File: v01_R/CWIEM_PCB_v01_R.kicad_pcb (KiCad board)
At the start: 2 copper layers, 50.8 x 50.8 mm, 46 parts, among them J1 USB, P1 CONN_1, P10 CONN_1, P11 CONN_1, P12 CONN_1, P2 CONN_1, P7 CONN_1, P8 CONN_1, P9 CONN_1, Q3 PNP, SW1 SW_PUSH_SMALL, U1 BC127, U2 TI_TPA6138A2, U4 MIC5219

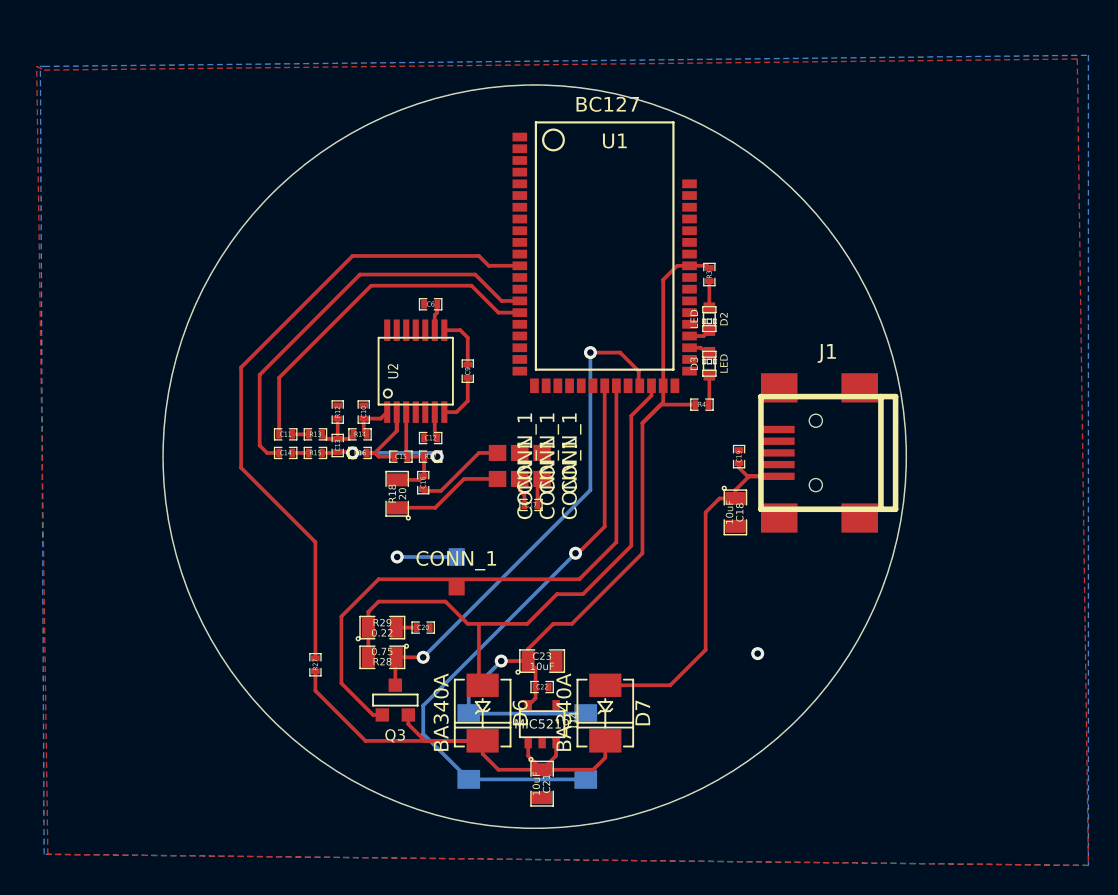
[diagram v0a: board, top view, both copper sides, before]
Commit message: Update with 2.00" diameter version of the CWIEM R v01 PCB. The only change remaining was to finalize sound driver pad placement and sizing. After that, production files could be generated for board manufacturing.
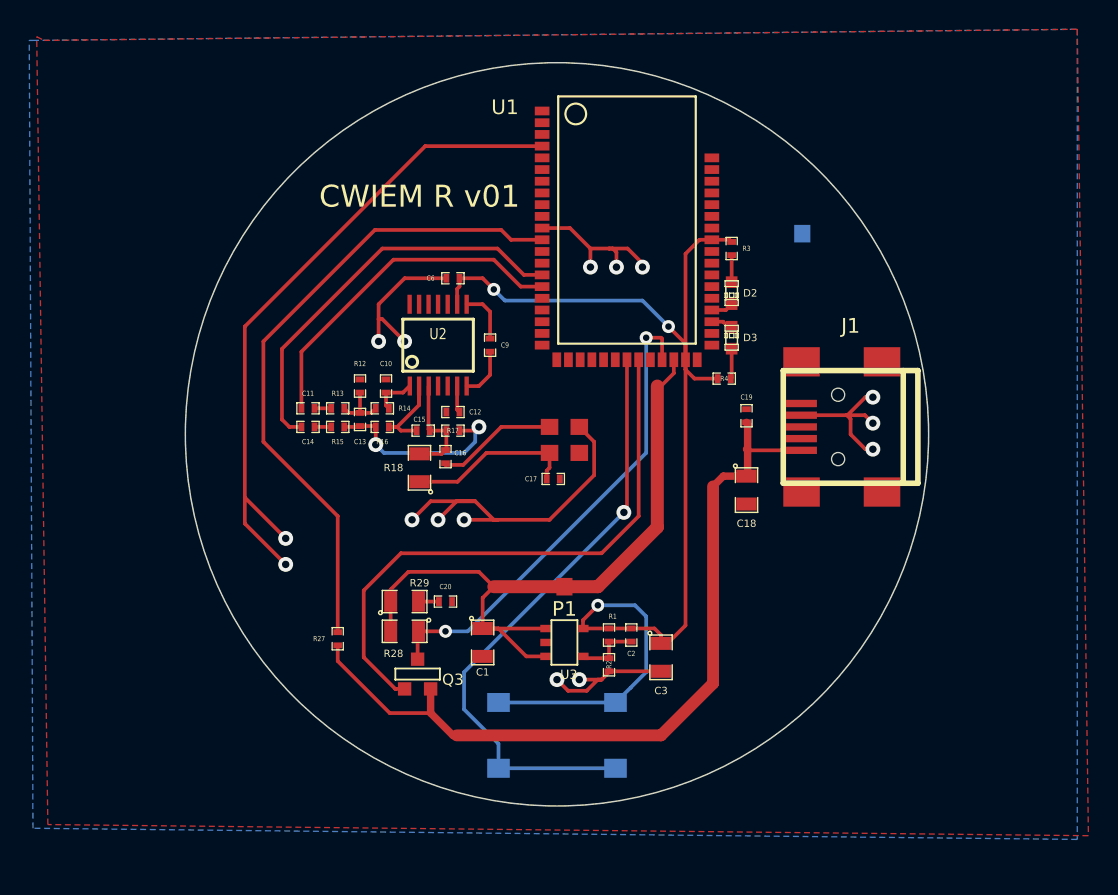
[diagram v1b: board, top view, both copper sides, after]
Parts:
- removed C21, C23: 10uF, SM0805
- removed C22: 1uF, SM0402_c
- removed D6, D7: BA340A, DO-214AC(SMA)
- removed P10, P11: CONN_1, BA Driver Pad
- removed U4: MIC5219, SOT23-5
- added C1: 10uF, SM0805, F.Cu at (72.6, 88.9)
- added C2: 1uF, SM0402_c, F.Cu at (82.8, 88.4)
- added C3: 10uF, SM0805, F.Cu at (84.8, 89.9)
- added R1: 52.3k, SM0402_r, F.Cu at (81.3, 88.4)
- added R2: 30.1k, SM0402_r, F.Cu at (81.3, 90.4)
- added U3: TPS73601DBVR, SOT23-5, F.Cu at (78.2, 88.9)
- R28: value 0.75 -> 0.8
- R29: value 0.22 -> 0.15
- U2: footprint tssop-14 -> TSSOP14
- moved P2 32.3 mm to (94.5, 61.0)
- moved P1 7.37 mm to (78.2, 85.1)
- moved P12 4.06 mm to (79.2, 75.9)
- moved P9 3.98 mm to (77.2, 75.9)
- moved P7 3.98 mm to (77.2, 74.2)
- moved P8 3.10 mm to (79.2, 74.2)
- moved C19 2.84 mm to (90.7, 73.4)
- moved C10 2.34 mm to (66.0, 71.4)
- moved C11 2.34 mm to (60.7, 72.9)
- moved C12 2.34 mm to (70.6, 73.2)
- moved C13 2.34 mm to (64.3, 73.7)
- moved C15 2.34 mm to (68.6, 74.4)
- moved C20 2.34 mm to (70.1, 86.1)
- moved C6 2.34 mm to (70.6, 64.0)
- moved C9 2.34 mm to (73.2, 68.6)
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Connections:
- C17 pad 1: N-0000050 (its old number) -> N-0000051
- C17 pad 2: N-0000052 (its old number) -> GND
- P9 pad 1: N-0000061 (its old number) -> N-0000051
- Q3 pad 1: VCHG -> 5V_USB
- R18 pad 1: N-0000061 (its old number) -> N-0000051
- R27 pad 2: VCHG -> 5V_USB
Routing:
- net GND: track 4.06 -> 112.3 mm, vias 1 -> 15
- net VCHG: track 36.0 -> 0.00 mm
- net 5V_USB: track 26.7 -> 55.6 mm
- net 3.3V: track 58.0 -> 81.0 mm, vias 1 -> 3
- net N-0000051: track 0.00 -> 11.6 mm
- net VBAT: track 40.0 -> 48.3 mm
- net N-0000061 (its old number): track 7.67 -> 0.00 mm
- net N-0000052: track 8.14 -> 13.5 mm
- net N-0000071: track 0.00 -> 4.49 mm
- net N-0000060: track 6.27 -> 8.31 mm
- net N-0000052 (its old number): track 1.91 -> 0.00 mm
- net N-0000050 (its old number): track 1.91 -> 0.00 mm
- net VBAT_SENSE: track 34.2 -> 33.0 mm
- net (no net): vias 1 -> 0
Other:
- board text added: "CWIEM R v01"

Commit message: Updating with CWIEM R v01 (1.8 inch diameter edition)
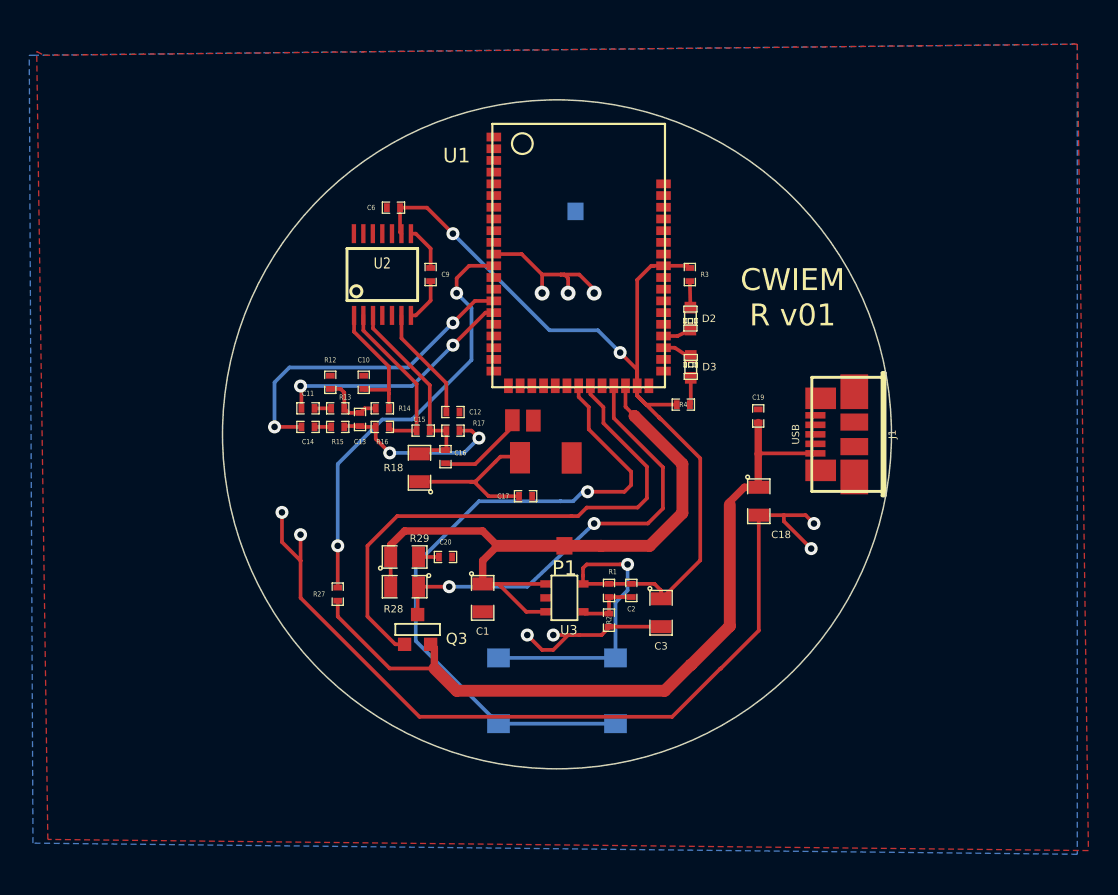
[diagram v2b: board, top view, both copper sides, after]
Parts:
- J1: footprint USB_MINI_B -> conn_usb_B_micro_smd
- P12, P9: footprint BA Driver Pad -> ci_pad
- P7, P8: footprint BA Driver Pad -> wbfk_pad
- moved P2 15.6 mm to (79.0, 59.4)
- moved C9 6.31 mm to (69.1, 63.8)
- moved C6 6.31 mm to (66.5, 59.2)
- moved U2 6.15 mm to (65.8, 63.8)
- moved U1 3.75 mm to (73.4, 54.4)
- moved D3 3.43 mm to (86.9, 70.1)
- moved R3 3.37 mm to (86.8, 63.8)
- moved D2 3.31 mm to (86.8, 66.8)
- moved R4 3.31 mm to (86.4, 72.6)
- moved P8 3.17 mm to (76.1, 73.7), turned to 180 degrees
- moved C1 3.05 mm to (72.6, 85.9)
- moved C2 3.05 mm to (82.8, 85.3)
- moved C3 3.05 mm to (84.8, 86.9)
- moved Q3 3.05 mm to (68.2, 88.0)
- moved R1 3.05 mm to (81.3, 85.3)
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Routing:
- net GND: track 112.3 -> 82.8 mm, vias 15 -> 9
- net AIO_1: track 44.5 -> 29.4 mm, vias 0 -> 2
- net SPKR_RP: track 23.7 -> 16.8 mm, vias 0 -> 2
- net N-0000062: track 7.45 -> 13.9 mm
- net N-0000050: track 2.94 -> 9.08 mm
- net N-0000055: track 1.84 -> 7.87 mm
- net SPKR_RN: track 27.7 -> 22.2 mm, vias 0 -> 2
- net VREGEN: track 41.5 -> 46.5 mm
- net N-0000061: track 7.27 -> 11.4 mm
- net 5V_USB: track 55.6 -> 52.8 mm
- net N-0000060: track 8.31 -> 5.65 mm
- net VBAT_SENSE: track 33.0 -> 30.6 mm
- net CHG_EXT: track 39.8 -> 37.9 mm
- net N-0000052: track 13.5 -> 12.4 mm
- net VBAT: track 48.3 -> 47.5 mm
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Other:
- board size 50.8 x 50.8 mm -> 45.7 x 45.7 mm

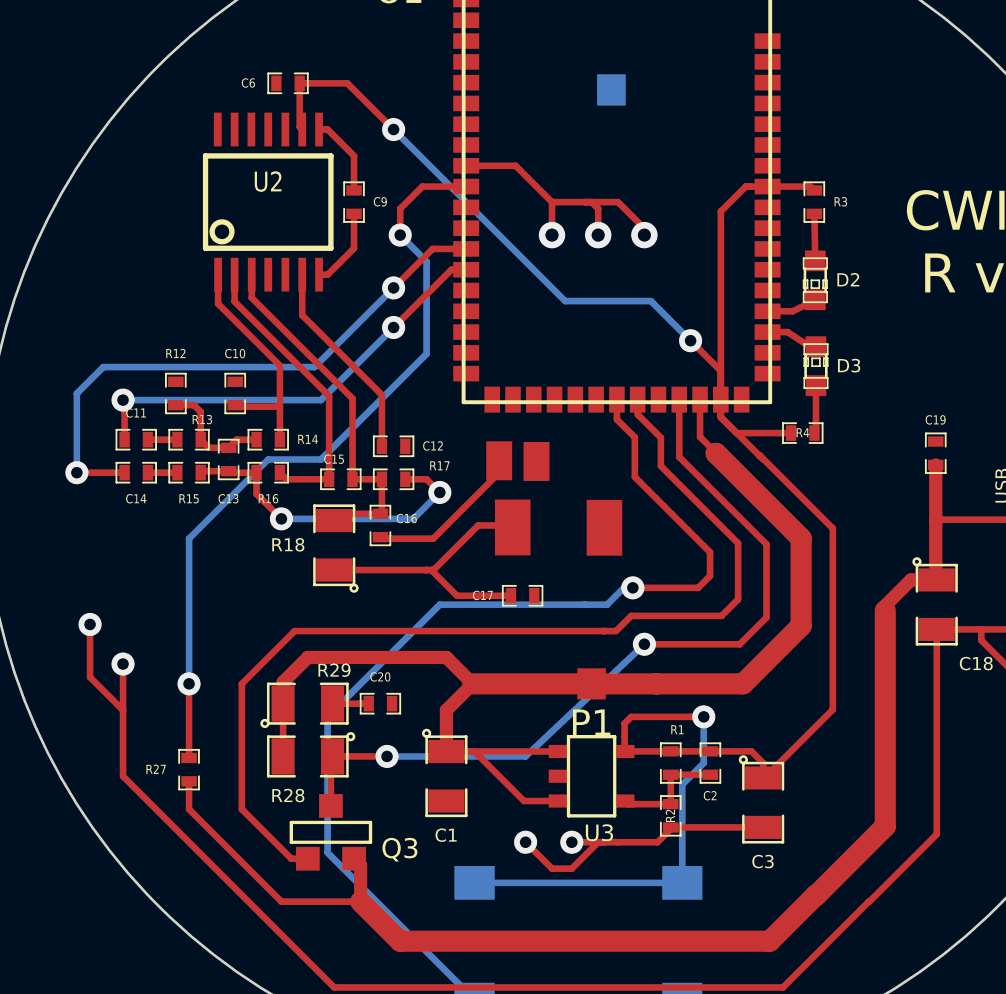
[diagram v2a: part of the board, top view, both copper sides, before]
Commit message: Updating PCB silkscreen (some part numbers were under the parts) and adding a zipped folder with first PCB files for order.
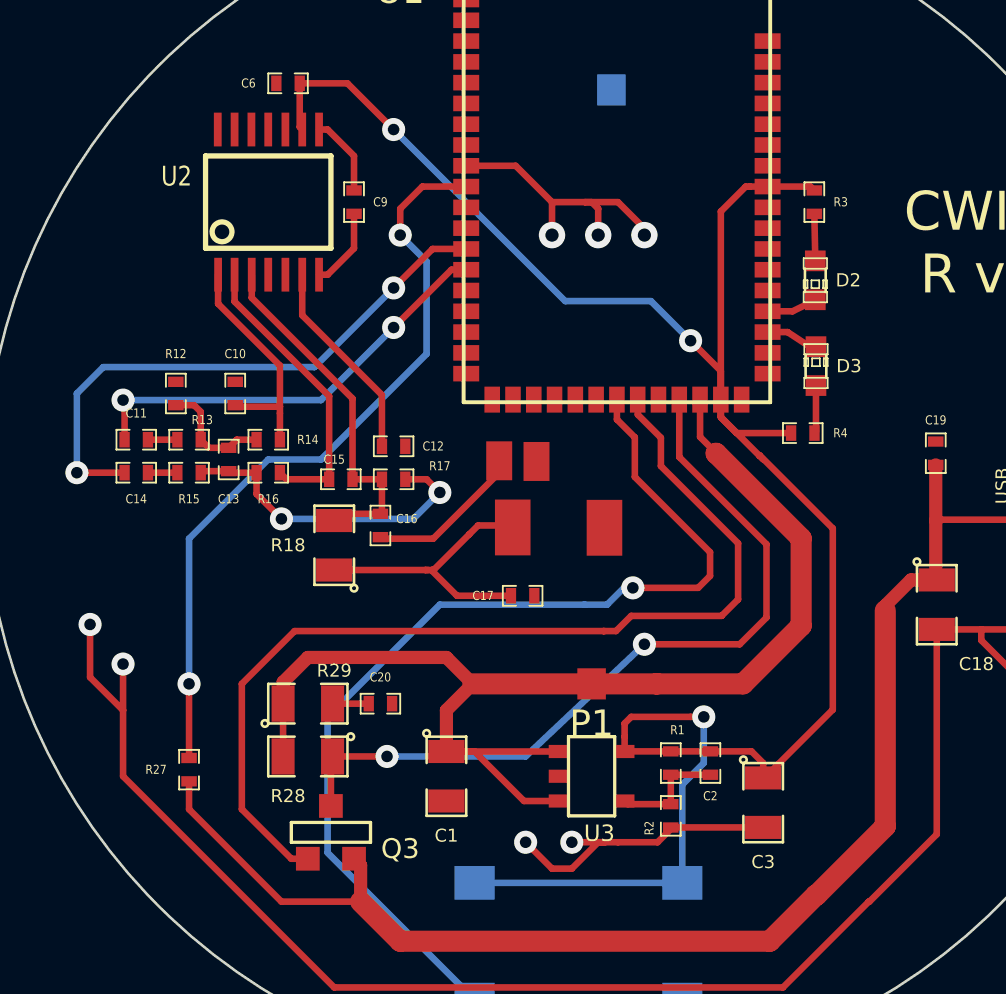
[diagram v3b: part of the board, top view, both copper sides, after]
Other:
- rule pad_to_mask_clearance: 0.05 -> 0.0508
- rule solder_mask_min_width: 0.05 -> 0.0508
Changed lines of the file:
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@@
     (pad_size 1.37 2.15)
     (pad_drill 0)
-    (pad_to_mask_clearance 0.05)
-    (solder_mask_min_width 0.05)
+    (pad_to_mask_clearance 0.0508)
+    (solder_mask_min_width 0.0508)
     (aux_axis_origin 0 0)
     (visible_elements 7FFFFFFF)
@@
       (drillshape 0)
       (scaleselection 1)
-      (outputdirectory ""))
+      (outputdirectory C:/Users/lifesatrip/Documents/TortoiseSVN/Wireless_IEMs/project001/trunk/v01_R/Gerbers/))
   )
   (net 0 "")
@@
     (at 86.36 72.644 180)
     (attr smd)
-    (fp_text reference R4 (at 0 0 180) (layer F.SilkS)
+    (fp_text reference R4 (at -1.4478 0 180) (layer F.SilkS)
       (effects (font (size 0.35052 0.3048) (thickness 0.07112)))
     )
@@
     (at 81.28 87.376 270)
     (attr smd)
-    (fp_text reference R2 (at 0 0 270) (layer F.SilkS)
+    (fp_text reference R2 (at 0.4699 0.8255 270) (layer F.SilkS)
       (effects (font (size 0.35052 0.3048) (thickness 0.07112)))
     )
@@
     (at 65.786 63.754)
     (attr smd)
-    (fp_text reference U2 (at 0 -0.762) (layer F.SilkS)
+    (fp_text reference U2 (at -3.5306 -0.9906) (layer F.SilkS)
       (effects (font (size 0.762 0.635) (thickness 0.16002)))
     )
